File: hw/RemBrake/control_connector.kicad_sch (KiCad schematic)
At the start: 8 parts, among them J4 Conn_01x08_MountingPin, J5 Conn_01x04_MountingPin, J6 Conn_01x03_MountingPin

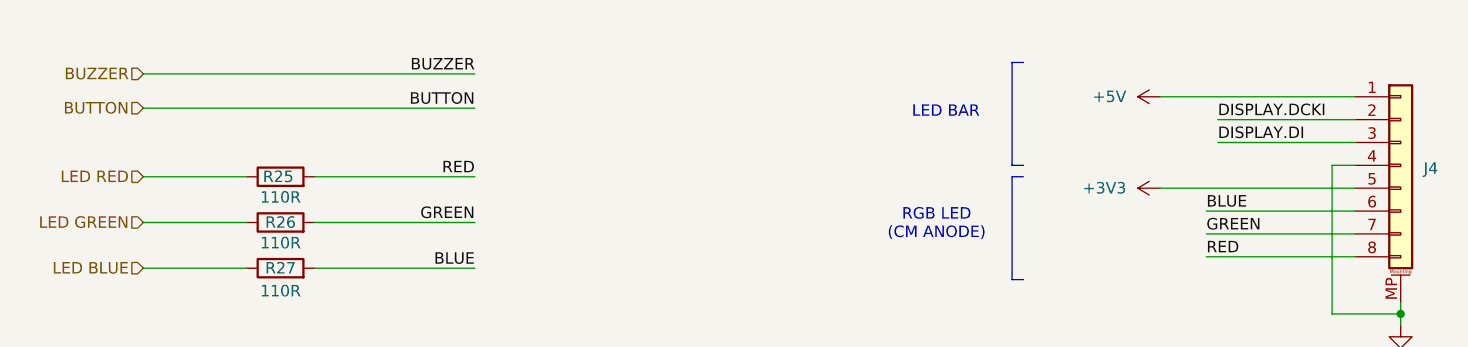
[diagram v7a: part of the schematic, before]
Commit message: fixed issue with the buzzer sound when charging is finished
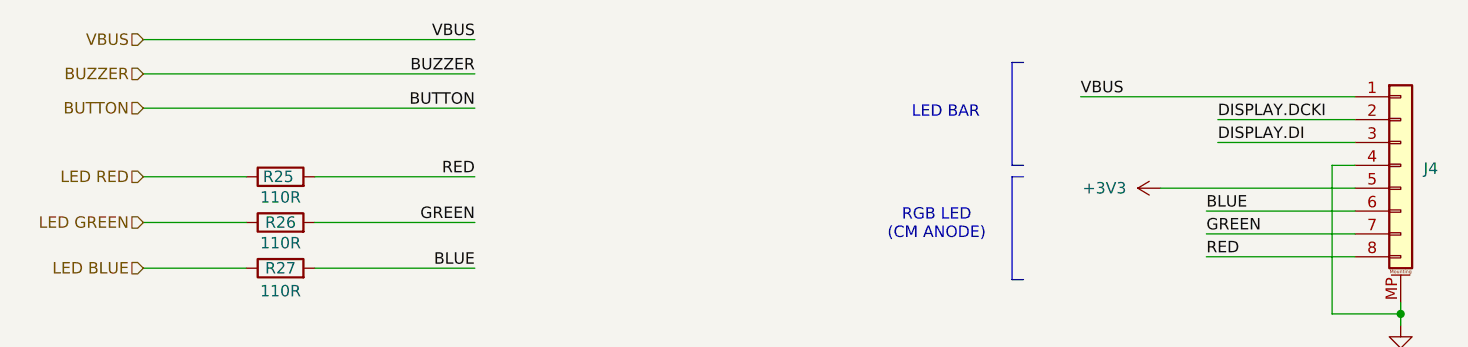
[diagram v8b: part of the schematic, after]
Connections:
- net +5V renamed VBUS
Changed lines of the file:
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@@
 	(wire
 		(pts
-			(xy 190.5 58.42) (xy 212.09 58.42)
+			(xy 77.47 52.07) (xy 114.3 52.07)
+		)
+		(stroke
+			(width 0)
+			(type default)
+		)
+	)
+	(wire
+		(pts
+			(xy 181.61 58.42) (xy 212.09 58.42)
 		)
 		(stroke
@@
 			(width 0)
 			(type default)
+		)
+	)
+	(label "VBUS"
+		(at 114.3 52.07 180)
+		(effects
+			(font
+				(size 1.27 1.27)
+			)
+			(justify right bottom)
 		)
 	)
@@
 	(label "I2C.SCL"
 		(at 199.39 101.6 0)
+		(effects
+			(font
+				(size 1.27 1.27)
+			)
+			(justify left bottom)
+		)
+	)
+	(label "VBUS"
+		(at 181.61 58.42 0)
 		(effects
 			(font
@@
 		(shape input)
 		(at 77.47 55.88 180)
+		(effects
+			(font
+				(size 1.27 1.27)
+			)
+			(justify right)
+		)
+	)
+	(hierarchical_label "VBUS"
+		(shape input)
+		(at 77.47 52.07 180)
 		(effects
 			(font
@@
 		(dnp no)
 		(fields_autoplaced yes)
-		(property "Reference" "#PWR026"
+		(property "Reference" "#PWR027"
 			(at 96.52 146.05 0)
 			(hide yes)
@@
 			(project "RemBrake"
 				(path "/e6d4ae5b-c9d7-4cbe-b288-c929fdf55a75/c6fda42a-9645-46e5-b66a-57cf8664dccf"
-					(reference "#PWR026")
+					(reference "#PWR027")
 					(unit 1)
 				)
@@
 		(dnp no)
 		(fields_autoplaced yes)
-		(property "Reference" "#PWR025"
+		(property "Reference" "#PWR026"
 			(at 86.36 146.05 0)
 			(hide yes)
@@
 			(project "RemBrake"
 				(path "/e6d4ae5b-c9d7-4cbe-b288-c929fdf55a75/c6fda42a-9645-46e5-b66a-57cf8664dccf"
-					(reference "#PWR025")
+					(reference "#PWR026")
 					(unit 1)
 				)
@@
 					(unit 1)
 				)
-			)
-		)
-	)
-	(symbol
-		(lib_id "power:+5V")
-		(at 190.5 58.42 90)
-		(unit 1)
-		(exclude_from_sim no)
-		(in_bom yes)
-		(on_board yes)
-		(dnp no)
-		(fields_autoplaced yes)
-		(property "Reference" "#PWR027"
-			(at 194.31 58.42 0)
-			(hide yes)
-			(effects
-				(font
-					(size 1.27 1.27)
-				)
-			)
-		)
-		(property "Value" "+5V"
-			(at 186.69 58.4199 90)
-			(effects
-				(font
-					(size 1.27 1.27)
-				)
-				(justify left)
-			)
-		)
-		(property "Footprint" ""
-			(at 190.5 58.42 0)
-			(hide yes)
-			(effects
-				(font
-					(size 1.27 1.27)
-				)
-			)
-		)
-		(property "Datasheet" ""
-			(at 190.5 58.42 0)
-			(hide yes)
-			(effects
-				(font
-					(size 1.27 1.27)
-				)
-			)
-		)
-		(property "Description" "Power symbol creates a global label with name \"+5V\""
-			(at 190.5 58.42 0)
-			(hide yes)
-			(effects
-				(font
-					(size 1.27 1.27)
-				)
-			)
-		)
-		(pin "1"
-		)
-		(instances
-			(project "RemBrake"
-				(path "/e6d4ae5b-c9d7-4cbe-b288-c929fdf55a75/c6fda42a-9645-46e5-b66a-57cf8664dccf"
-					(reference "#PWR027")
-					(unit 1)
-				)
